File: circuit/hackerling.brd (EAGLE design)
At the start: 82.5 x 67.4 mm, 42 parts, among them IC1 MCP23017SP, IC2 MCP2300X/P, IC3 MIC5219BM5, SW2 SWITCH_B13EH, U1 MMA8452Q, U2 LCD_16X2, U3 ARDUINOR3-BPLACE, U4 ACCELEROMETER, U5 PCA9306, U6 ACCELEROMETER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

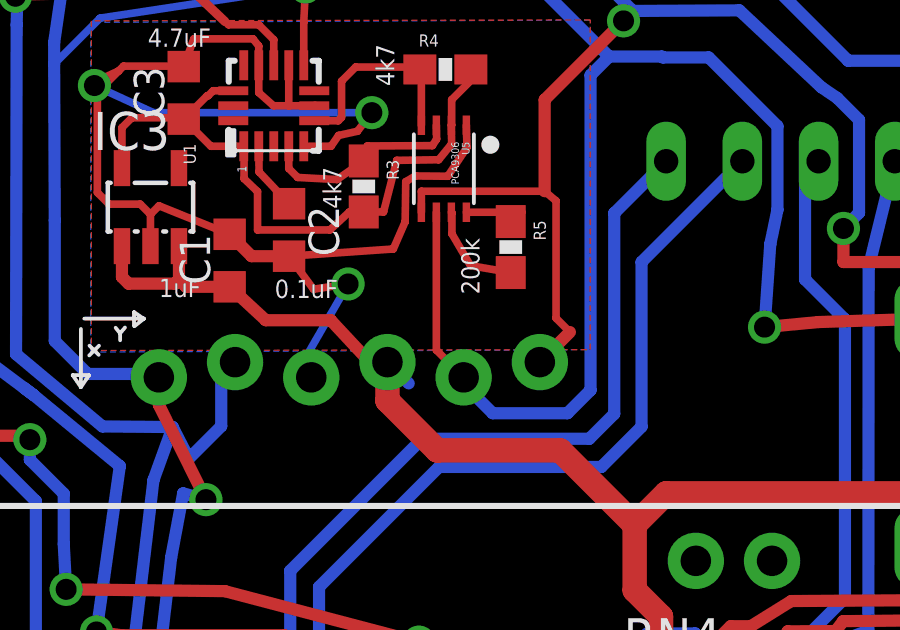
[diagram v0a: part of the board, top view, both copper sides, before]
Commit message: power change to accelerometer section
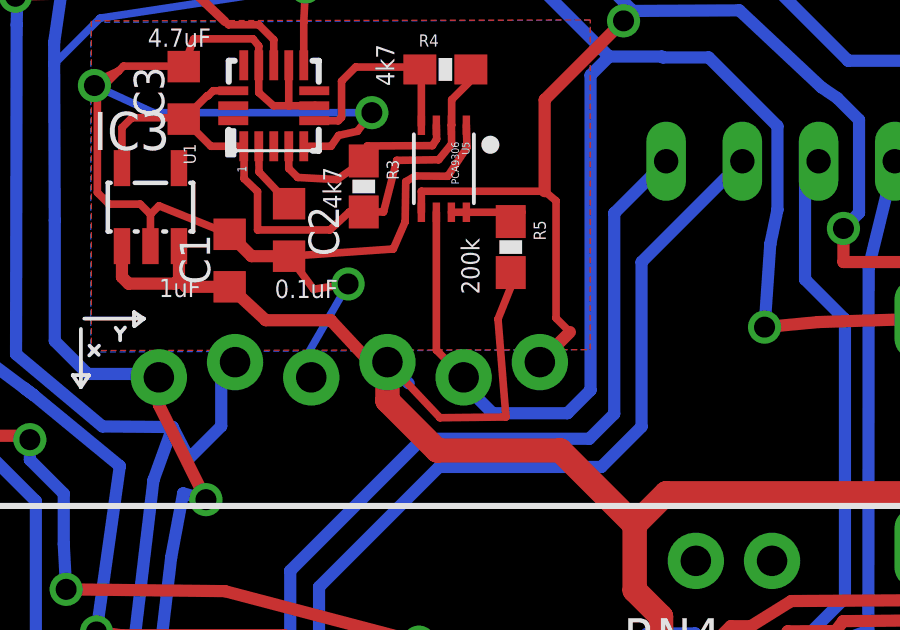
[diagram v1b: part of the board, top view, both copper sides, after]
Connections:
- removed net 5V: R5.2, U5.P$7
- removed net N$27: R5.1, U5.P$8
- new net N$5: R5.1, U5.P$7, U5.P$8
- net VCC: now also R5.2
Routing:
- net VCC: track 341.6 -> 351.3 mm
- net 5V: track 3.32 -> 0.00 mm
- net N$5: track 0.00 -> 2.83 mm
- net N$27: track 2.33 -> 0.00 mm
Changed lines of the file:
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@@
 <?xml version="1.0" encoding="utf-8"?>
 <!DOCTYPE eagle SYSTEM "eagle.dtd">
-<eagle version="6.2">
+<eagle version="6.4">
 <drawing>
 <settings>
@@
 <layer number="19" name="Unrouted" color="6" fill="1" visible="yes" active="yes"/>
 <layer number="20" name="Dimension" color="15" fill="1" visible="yes" active="yes"/>
-<layer number="21" name="tPlace" color="7" fill="1" visible="no" active="yes"/>
+<layer number="21" name="tPlace" color="7" fill="1" visible="yes" active="yes"/>
 <layer number="22" name="bPlace" color="7" fill="1" visible="yes" active="yes"/>
 <layer number="23" name="tOrigins" color="15" fill="1" visible="yes" active="yes"/>
@@
 <layer number="111" name="LPC17xx" color="7" fill="1" visible="no" active="yes"/>
 <layer number="112" name="tSilk" color="7" fill="1" visible="no" active="yes"/>
-<layer number="113" name="binstruct" color="13" fill="1" visible="yes" active="yes"/>
+<layer number="113" name="binstruct" color="13" fill="1" visible="no" active="yes"/>
 <layer number="114" name="tInstruct" color="5" fill="1" visible="no" active="yes"/>
-<layer number="115" name="bGeneralInstruct" color="13" fill="1" visible="yes" active="yes"/>
+<layer number="115" name="bGeneralInstruct" color="13" fill="1" visible="no" active="yes"/>
 <layer number="116" name="Patch_BOT" color="9" fill="4" visible="yes" active="yes"/>
 <layer number="121" name="_tsilk" color="7" fill="1" visible="yes" active="yes"/>
@@
 </class>
 </classes>
-<designrules>
+<designrules name="default">
 <description language="de">&lt;b&gt;EAGLE Design Rules&lt;/b&gt;
 &lt;p&gt;
@@
 <wire x1="43.83" y1="11.733" x2="43.84" y2="11.87" width="0.8128" layer="1"/>
 <wire x1="43.84" y1="11.87" x2="43.84" y2="16.23" width="0.8128" layer="1"/>
+<contactref element="R5" pad="2"/>
+<wire x1="29.82" y1="43.58" x2="29.88" y2="43.265" width="0.254" layer="1"/>
+<wire x1="29.88" y1="43.265" x2="29.88" y2="43.24" width="0.254" layer="1"/>
+<wire x1="29.88" y1="43.24" x2="29.395" y2="42.03" width="0.254" layer="1"/>
+<wire x1="29.395" y1="42.03" x2="29.66" y2="38.765" width="0.254" layer="1"/>
+<wire x1="29.66" y1="38.765" x2="27.459" y2="38.74" width="0.254" layer="1"/>
+<wire x1="27.459" y1="38.74" x2="25.71" y2="40.594" width="0.254" layer="1"/>
 </signal>
 <signal name="VIN">
@@
 <wire x1="27.85" y1="48.5" x2="27.84" y2="48.49" width="0.254" layer="1"/>
 </signal>
-<signal name="5V">
-<contactref element="U5" pad="P$7"/>
-<contactref element="R5" pad="2"/>
-<wire x1="29.82" y1="43.58" x2="28.48" y2="43.81" width="0.254" layer="1"/>
-<wire x1="28.48" y1="43.81" x2="27.86" y2="44.87" width="0.254" layer="1"/>
-<wire x1="27.86" y1="44.87" x2="27.86" y2="45.57" width="0.254" layer="1"/>
-<wire x1="27.86" y1="45.57" x2="27.84" y2="45.59" width="0.254" layer="1"/>
-</signal>
 <signal name="SCL_3">
 <contactref element="U5" pad="P$3"/>
@@
 <wire x1="21.42" y1="47.79" x2="21.43" y2="46.935" width="0.254" layer="1"/>
 <wire x1="21.43" y1="46.935" x2="22.43" y2="45.875" width="0.254" layer="1"/>
-</signal>
-<signal name="N$27">
-<contactref element="U5" pad="P$8"/>
-<contactref element="R5" pad="1"/>
-<wire x1="28.34" y1="45.59" x2="30.19" y2="45.59" width="0.254" layer="1"/>
-<wire x1="30.19" y1="45.59" x2="29.82" y2="45.28" width="0.254" layer="1"/>
 </signal>
 <signal name="N$21">
@@
 <wire x1="29.38" y1="30.37" x2="33.28" y2="30.35" width="0.4064" layer="16"/>
 </signal>
+<signal name="N$5">
+<contactref element="U5" pad="P$7"/>
+<contactref element="U5" pad="P$8"/>
+<contactref element="R5" pad="1"/>
+<wire x1="28.34" y1="45.59" x2="30.19" y2="45.59" width="0.254" layer="1"/>
+<wire x1="30.19" y1="45.59" x2="29.82" y2="45.28" width="0.254" layer="1"/>
+<wire x1="28.34" y1="45.59" x2="27.84" y2="45.59" width="0.254" layer="1"/>
+</signal>
 </signals>

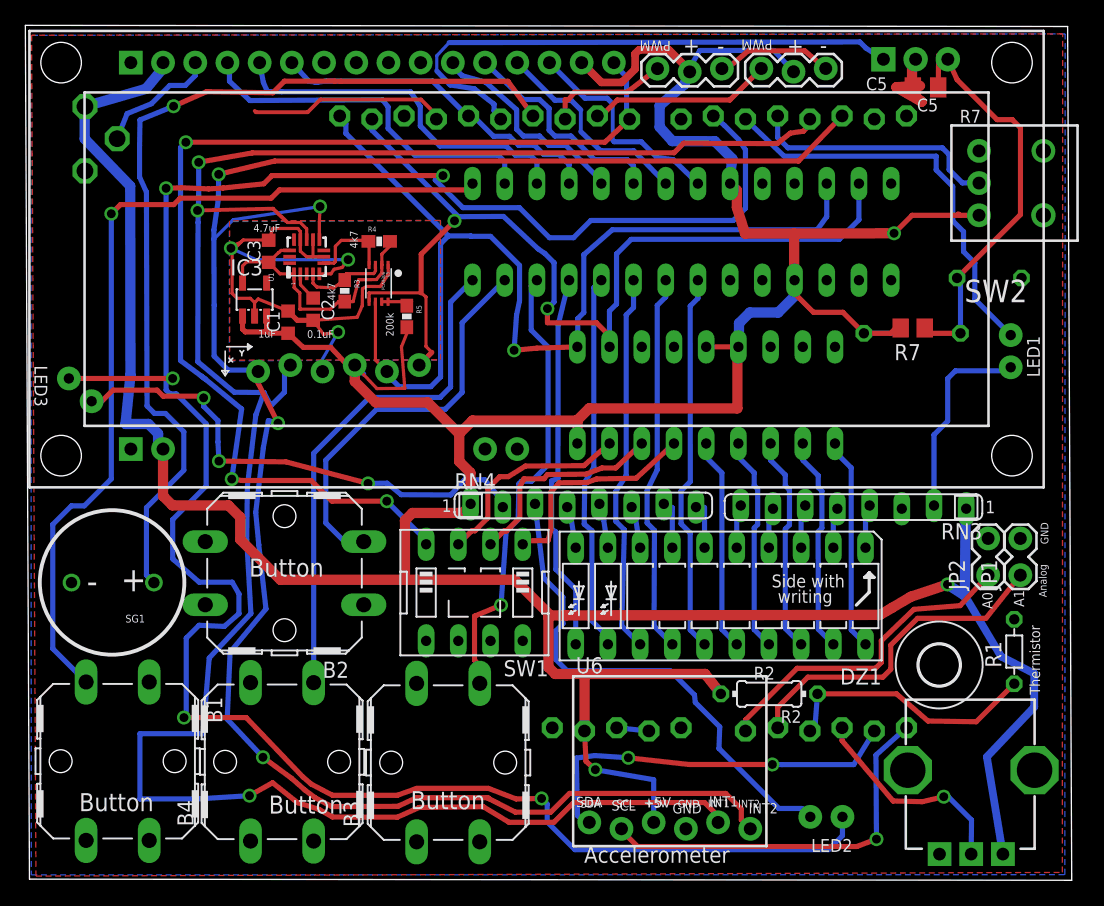
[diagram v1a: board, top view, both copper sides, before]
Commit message: removing optional components
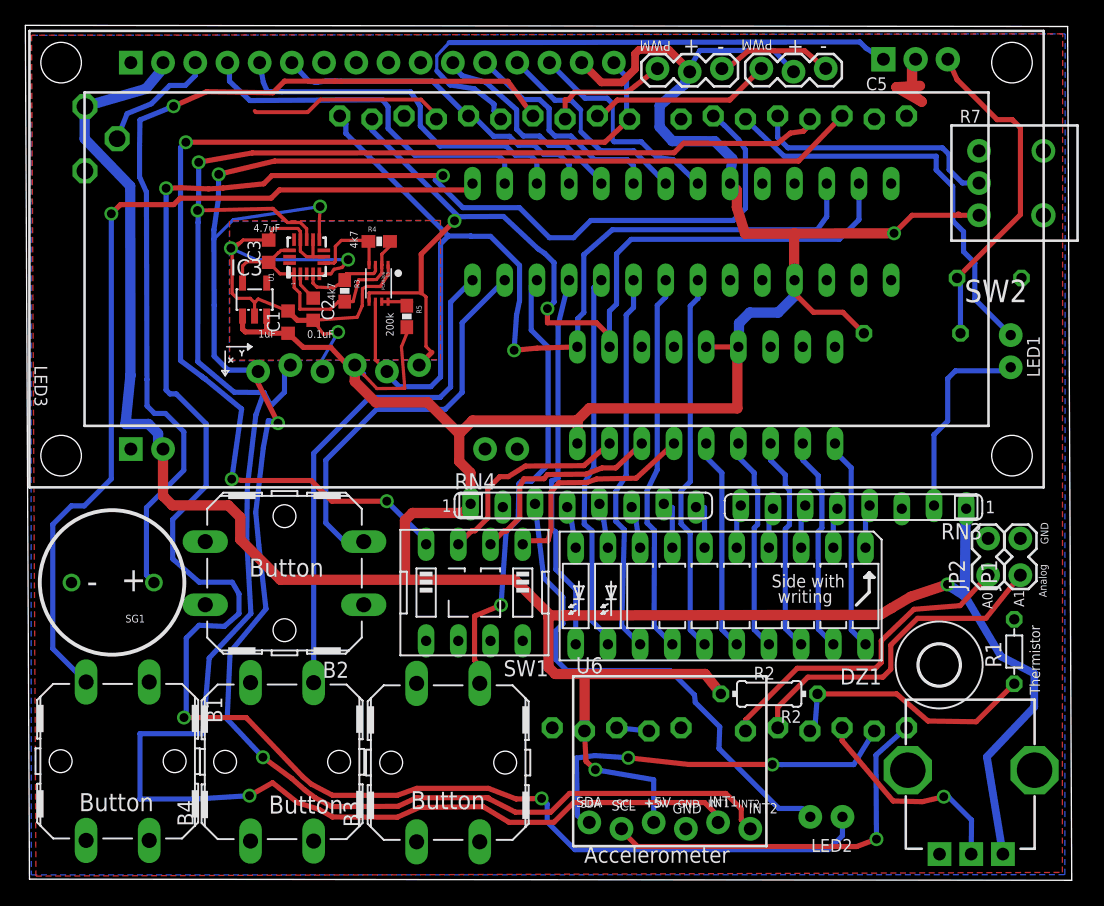
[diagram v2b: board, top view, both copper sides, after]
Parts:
- removed C5: 10uF, resistor:C0805K
- removed LED3: (no value), SparkFun:LED5MM
- removed R7: (no value), rcl:R0805
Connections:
- net GND: no longer C5.2
- net IR_OUT1: no longer LED3.K
- net N$19: no longer C5.1, R7.1
- net N$32: no longer LED3.A
- net VCC: no longer R7.2
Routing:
- net N$32: track 39.6 -> 0.00 mm, vias 3 -> 0
- net IR_OUT1: track 177.5 -> 168.8 mm, vias 5 -> 4
- net VCC: track 351.3 -> 345.7 mm
- net N$19: track 33.1 -> 27.5 mm
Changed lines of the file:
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@@
 <element name="C4" library="rcl" package="C050-050X075" value="10uF" x="75.76" y="47.46" rot="MR180"/>
 <element name="R6" library="resistor" package="0204/7" value="47" x="69.68" y="43.1" rot="MR0"/>
-<element name="R7" library="rcl" package="R0805" value="" x="69.72" y="43.52" rot="R180"/>
-<element name="C5" library="resistor" package="C0805K" value="10uF" x="70.73" y="62.49" rot="R180"/>
 <element name="JP1" library="SparkFun" package="1X02_LOCK" value="" x="78.21" y="24.2" rot="R90"/>
 <element name="JP2" library="SparkFun" package="1X02_LOCK" value="" x="75.67" y="24.2" rot="R90"/>
-<element name="LED3" library="SparkFun" package="LED5MM" value="" x="4.06" y="38.64" rot="MR45"/>
 </elements>
 <signals>
@@
 <wire x1="22.81" y1="40.446" x2="23.17" y2="40.086" width="0.254" layer="16"/>
 <contactref element="C4" pad="2"/>
-<contactref element="C5" pad="2"/>
 <wire x1="17.81" y1="44.4599" x2="17.81" y2="45.52" width="0.254" layer="1"/>
 <wire x1="17.81" y1="45.52" x2="17.47" y2="45.86" width="0.254" layer="1"/>
@@
 <wire x1="25.74" y1="40.594" x2="25.74" y2="40.64" width="0.254" layer="1"/>
 <contactref element="R6" pad="2"/>
-<wire x1="65.87" y1="43.1" x2="68.21" y2="43.1" width="0.4064" layer="16"/>
-<wire x1="68.21" y1="43.1" x2="68.39" y2="43.28" width="0.4064" layer="16"/>
-<contactref element="R7" pad="2"/>
 <wire x1="74.95" y1="52.41" x2="74.73" y2="52.41" width="0.4064" layer="1"/>
 <wire x1="25.74" y1="40.64" x2="25.08" y2="40.64" width="0.4064" layer="1"/>
@@
 <wire x1="35" y1="36.22" x2="43.24" y2="36.22" width="0.8128" layer="1"/>
 <wire x1="43.24" y1="36.22" x2="43.29" y2="36.27" width="0.8128" layer="1"/>
-<wire x1="68.77" y1="43.52" x2="68.4" y2="43.52" width="0.4064" layer="1"/>
-<wire x1="68.4" y1="43.52" x2="67.98" y2="43.1" width="0.4064" layer="1"/>
-<wire x1="67.98" y1="43.1" x2="65.87" y2="43.1" width="0.4064" layer="1"/>
 <wire x1="33.95" y1="35.17" x2="31.47" y2="37.65" width="0.8128" layer="1"/>
 <wire x1="31.47" y1="37.65" x2="27.37" y2="37.65" width="0.8128" layer="1"/>
@@
 <wire x1="12.05" y1="54.58" x2="10.83" y2="54.54" width="0.4064" layer="1"/>
 <via x="10.83" y="54.54" extent="1-16" drill="0.7"/>
-<wire x1="10.83" y1="54.54" x2="10.83" y2="39.54" width="0.4064" layer="16"/>
-<wire x1="10.83" y1="39.54" x2="10.83" y2="38.63" width="0.4064" layer="16"/>
+<wire x1="10.83" y1="54.54" x2="10.83" y2="38.63" width="0.4064" layer="16"/>
 <wire x1="11.43" y1="25.24" x2="13.44" y2="23.47" width="0.4064" layer="16"/>
 <wire x1="13.44" y1="23.47" x2="16.05" y2="23.47" width="0.4064" layer="16"/>
@@
 <wire x1="13.99" y1="35.96" x2="11.63" y2="38.32" width="0.4064" layer="16"/>
 <wire x1="11.63" y1="38.32" x2="11.14" y2="38.32" width="0.4064" layer="16"/>
-<via x="11.35" y="39.54" extent="1-16" drill="0.7"/>
-<wire x1="11.35" y1="39.54" x2="10.83" y2="39.54" width="0.4064" layer="16"/>
-<contactref element="LED3" pad="K"/>
-<wire x1="3.161975" y1="39.538025" x2="11.348025" y2="39.538025" width="0.4064" layer="1"/>
-<wire x1="11.348025" y1="39.538025" x2="11.35" y2="39.54" width="0.4064" layer="1"/>
 <contactref element="U3" pad="D6"/>
 <wire x1="53.99" y1="60.247" x2="54.86" y2="59.51" width="0.4064" layer="16"/>
@@
 </signal>
 <signal name="N$19">
-<contactref element="C5" pad="1"/>
-<contactref element="R7" pad="1"/>
 <contactref element="IR1" pad="3"/>
 <contactref element="IR1" pad="3"/>
@@
 <wire x1="73.49" y1="47.19" x2="73.22" y2="47.46" width="0.4064" layer="16"/>
 <wire x1="72.49" y1="64.715" x2="71.77" y2="65.03" width="0.4064" layer="1"/>
-<wire x1="71.77" y1="65.03" x2="71.73" y2="62.49" width="0.4064" layer="1"/>
-<wire x1="73.49" y1="43.1" x2="71.09" y2="43.1" width="0.4064" layer="1"/>
-<wire x1="71.09" y1="43.1" x2="70.67" y2="43.52" width="0.4064" layer="1"/>
 <wire x1="72.49" y1="64.715" x2="73.22" y2="63.11" width="0.4064" layer="1"/>
 <wire x1="73.22" y1="63.11" x2="76.38" y2="59.95" width="0.4064" layer="1"/>
@@
 </signal>
 <signal name="N$32">
-<contactref element="LED3" pad="A"/>
 <contactref element="RN4" pad="2"/>
-<wire x1="37.39" y1="29.393" x2="37.15" y2="30.1" width="0.4064" layer="16"/>
-<wire x1="37.15" y1="30.1" x2="35.97" y2="31.55" width="0.4064" layer="16"/>
-<wire x1="35.97" y1="31.55" x2="34.37" y2="31.55" width="0.4064" layer="16"/>
-<wire x1="34.37" y1="31.55" x2="33.28" y2="30.35" width="0.4064" layer="16"/>
-<wire x1="4.958028125" y1="37.741971875" x2="5.761971875" y2="37.741971875" width="0.4064" layer="1"/>
-<wire x1="5.761971875" y1="37.741971875" x2="6.64" y2="38.62" width="0.4064" layer="1"/>
-<wire x1="6.64" y1="38.62" x2="10.12" y2="38.62" width="0.4064" layer="1"/>
-<wire x1="10.12" y1="38.62" x2="10.6" y2="38.14" width="0.4064" layer="1"/>
-<wire x1="10.6" y1="38.14" x2="13.66" y2="38.14" width="0.4064" layer="1"/>
-<wire x1="13.66" y1="38.14" x2="13.79" y2="38.01" width="0.4064" layer="1"/>
-<via x="13.79" y="38.01" extent="1-16" drill="0.7"/>
-<wire x1="13.79" y1="38.01" x2="13.79" y2="37.34" width="0.4064" layer="16"/>
-<wire x1="13.79" y1="37.34" x2="14.92" y2="36.21" width="0.4064" layer="16"/>
-<wire x1="14.92" y1="36.21" x2="14.92" y2="34.53" width="0.4064" layer="16"/>
-<wire x1="14.92" y1="34.53" x2="15" y2="33.02" width="0.4064" layer="16"/>
-<via x="15" y="33.02" extent="1-16" drill="0.7"/>
-<wire x1="15" y1="33.02" x2="20.29" y2="32.96" width="0.4064" layer="1"/>
-<wire x1="20.29" y1="32.96" x2="26.76" y2="31.26" width="0.4064" layer="1"/>
-<via x="26.76" y="31.26" extent="1-16" drill="0.7"/>
-<wire x1="26.76" y1="31.26" x2="28.26" y2="31.28" width="0.4064" layer="16"/>
-<wire x1="28.26" y1="31.28" x2="29.38" y2="30.37" width="0.4064" layer="16"/>
-<wire x1="29.38" y1="30.37" x2="33.28" y2="30.35" width="0.4064" layer="16"/>
 </signal>
 <signal name="N$5">

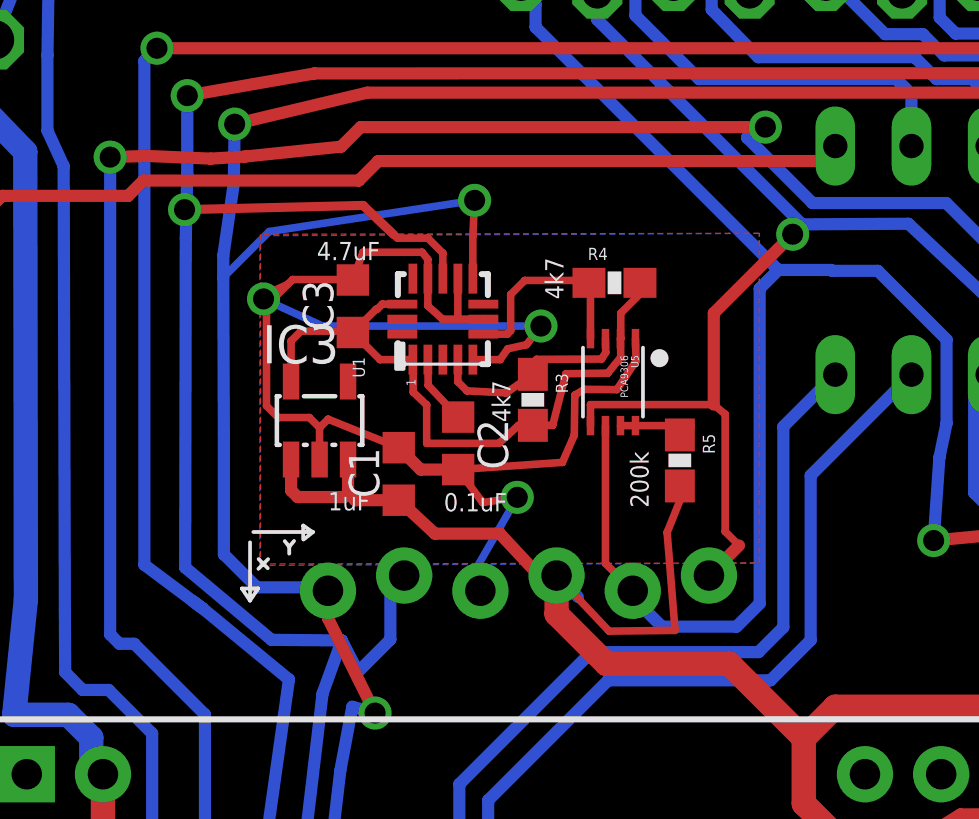
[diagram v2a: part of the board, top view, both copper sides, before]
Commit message: adding resistors to interrupt
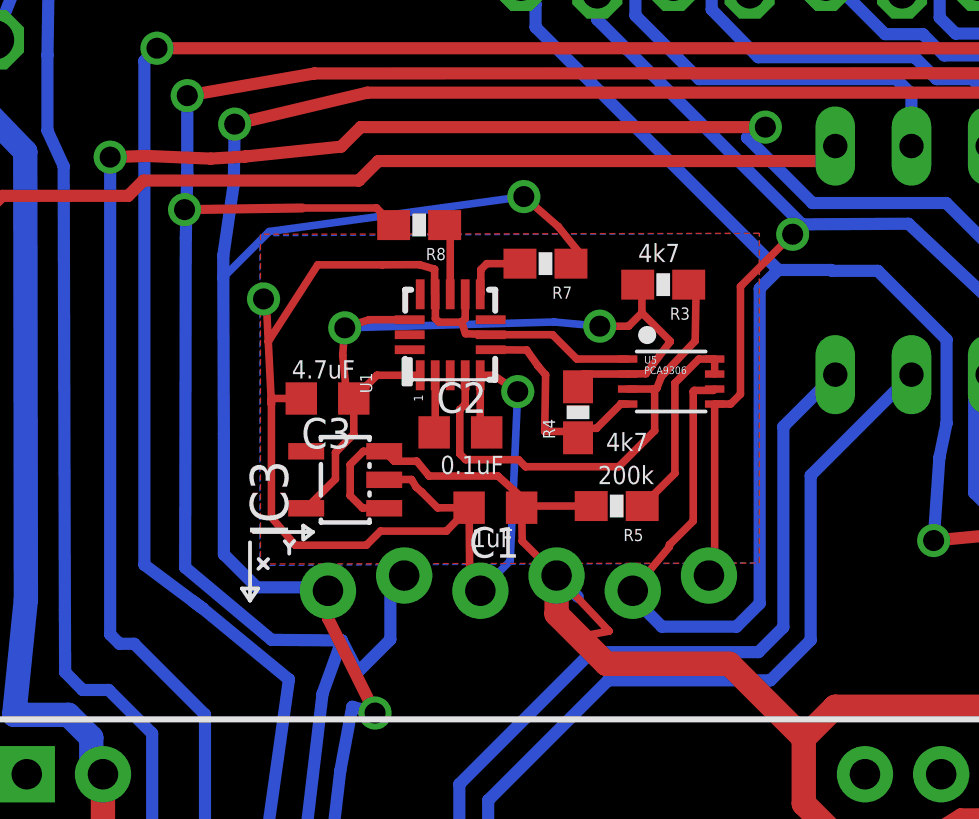
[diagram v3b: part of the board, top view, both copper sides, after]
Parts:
- added R7, R8: 500, SparkFun:0603-RES
- moved R3 5.80 mm to (29.3, 50.3), turned to 180 degrees
- moved R4 4.48 mm to (26.4, 46.0), turned to 90 degrees
- moved C1 3.41 mm to (23.7, 42.9), turned to 180 degrees
- moved C3 3.19 mm to (18.1, 46.5), turned to 180 degrees
- moved R5 2.60 mm to (27.7, 42.9), turned to 180 degrees
- moved IC3 2.15 mm to (18.7, 43.8), turned to 90 degrees
- moved U5 1.94 mm to (29.5, 47.1), turned to 270 degrees
- moved U1 0.57 mm to (22.2, 48.6)
- moved C2 0.37 mm to (22.5, 45.4), turned to 0 degrees
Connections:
- new net N$6: R7.2, U1.9
- new net N$7: R8.1, U1.11
- net A_INT1: now also R8.2; no longer U1.11
- net A_INT2: now also R7.1; no longer U1.9
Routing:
- net SCL_3: track 6.97 -> 16.3 mm
- net 3.3V: track 22.0 -> 27.9 mm, vias 0 -> 2
- net SDA: track 80.4 -> 75.1 mm
- net N$5: track 2.83 -> 6.71 mm
- net VCC: track 345.7 -> 341.9 mm
- net A_INT1: track 174.3 -> 171.4 mm
- net N$7: track 0.00 -> 2.38 mm
- net SCL: track 84.8 -> 87.1 mm
- net N$6: track 0.00 -> 2.22 mm
- net A_INT2: track 158.2 -> 160.3 mm
- net GND: track 88.3 -> 86.3 mm, vias 3 -> 2
- net SDA_3: track 6.88 -> 7.53 mm
